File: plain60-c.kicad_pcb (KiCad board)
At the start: 2 copper layers, 284.7 x 94.2 mm, 165 parts, among them J2 ISP, J3 ai03_ud, K1 KEYSW, K10 KEYSW, K11 KEYSW, K12 KEYSW, K13 KEYSW, K14 KEYSW, K15 KEYSW, K15-1 KEYSW, K16 KEYSW, K17 KEYSW, K18 KEYSW, K19 KEYSW, K2 KEYSW, K20 KEYSW, K21 KEYSW, K22 KEYSW, K23 KEYSW, K24 KEYSW, K25 KEYSW, K26 KEYSW, K27 KEYSW, K28 KEYSW, K29 KEYSW, K3 KEYSW, K31 KEYSW, K31-1 KEYSW, K32 KEYSW, K33 KEYSW, K34 KEYSW, K35 KEYSW, K36 KEYSW, K37 KEYSW, K38 KEYSW, K39 KEYSW, K4 KEYSW, K40 KEYSW, K41 KEYSW, K42 KEYSW, K43 KEYSW, K44 KEYSW, K44-1 KEYSW, K46 KEYSW, K46-1 KEYSW, K47 KEYSW, K48 KEYSW, K49 KEYSW, K5 KEYSW, K50 KEYSW, K51 KEYSW, K52 KEYSW, K53 KEYSW, K54 KEYSW, K55 KEYSW, K56 KEYSW, K57 KEYSW, K58 KEYSW, K58-1 KEYSW, K59 KEYSW, K6 KEYSW, K61 KEYSW, K61-1 KEYSW, K62 KEYSW, K62-1 KEYSW, K63 KEYSW, K63-1 KEYSW, K67 KEYSW, K67-1 KEYSW, K7 KEYSW, K71 KEYSW, K72 KEYSW, K72-1 KEYSW, K73 KEYSW, K73-1 KEYSW, K74 KEYSW, K74-1 KEYSW, K8 KEYSW, K9 KEYSW, SW1 SW_PUSH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

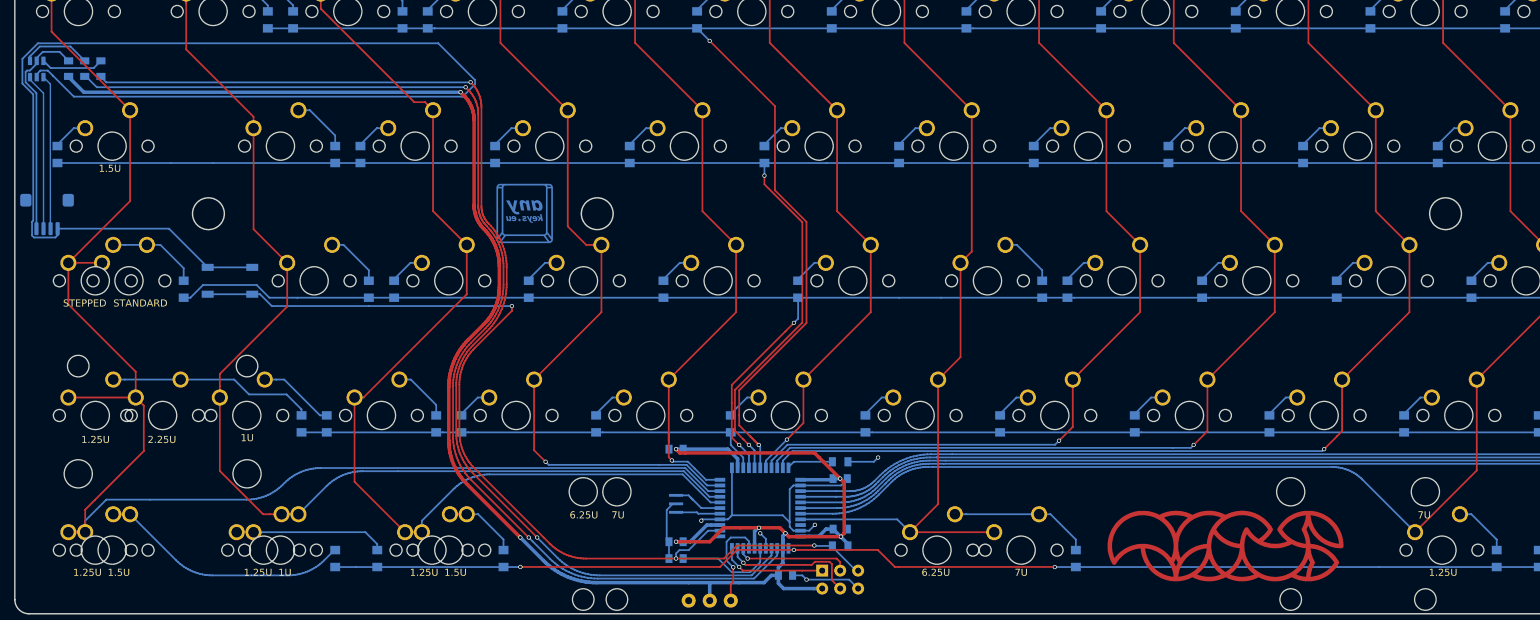
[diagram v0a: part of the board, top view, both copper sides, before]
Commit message: fixed some traces and redo gerber
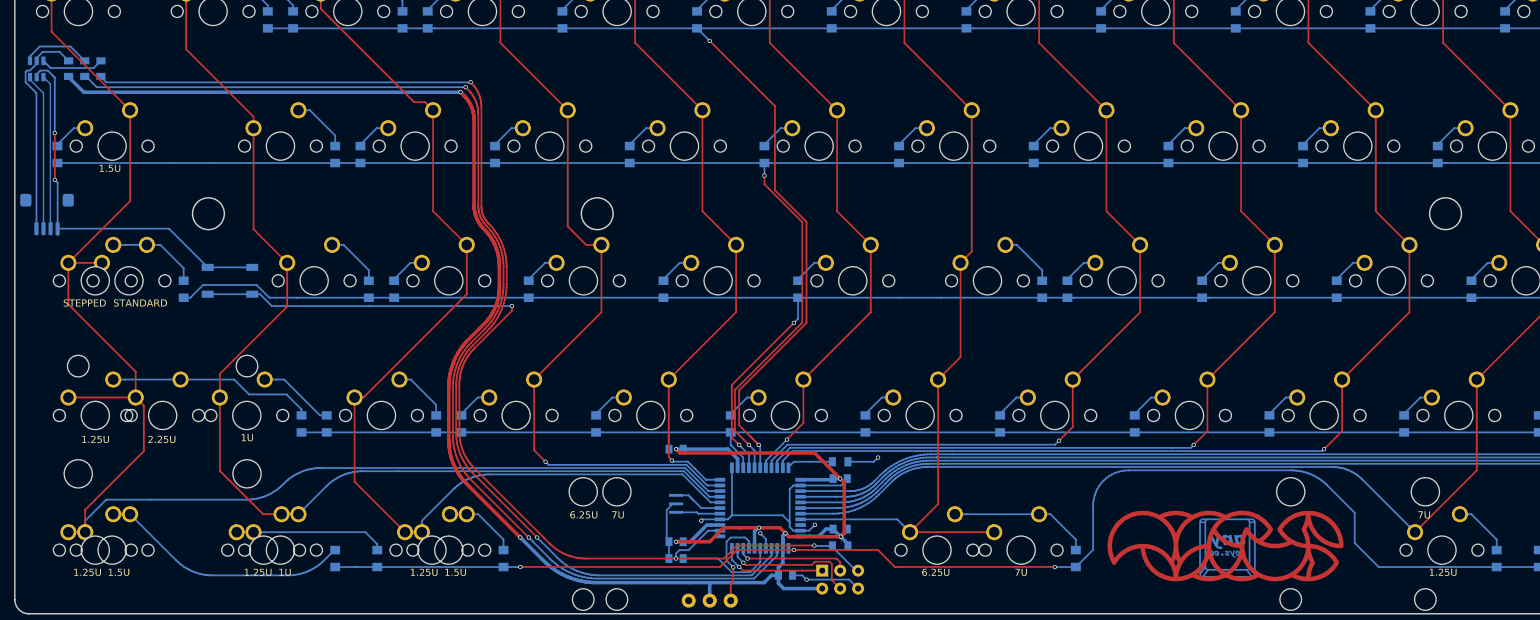
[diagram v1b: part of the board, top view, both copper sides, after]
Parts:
- moved G*** 132.4 mm to (163.1, 85.4)
- moved G*** 110.1 mm to (172.1, 85.4)
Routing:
- net GND: track 257.7 -> 120.6 mm, vias 5 -> 7
- net row4: track 196.9 -> 214.9 mm
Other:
- board text removed: "Noctus edition"

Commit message: add side cuts
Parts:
- moved G*** 0.74 mm to (163.1, 86.2)
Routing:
- net GND: track 120.6 -> 318.1 mm, vias 7 -> 11
- net row4: track 214.9 -> 234.2 mm
- net col10: track 184.7 -> 189.6 mm
- net RST: track 139.9 -> 144.0 mm
- net VCC: track 278.3 -> 275.2 mm
- net row0: track 288.2 -> 286.9 mm
- net col4: track 87.9 -> 86.6 mm
- net D+: track 21.9 -> 22.8 mm, vias 0 -> 2
- net VBUS: track 31.1 -> 30.4 mm, vias 0 -> 2
- net Net-(U1-Pad17): track 7.45 -> 6.95 mm
- net D-: vias 0 -> 2
- added copper zone on F.Cu, net (none)
- added copper zone on B.Cu, net GND
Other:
- outline, holes or cut-outs redrawn

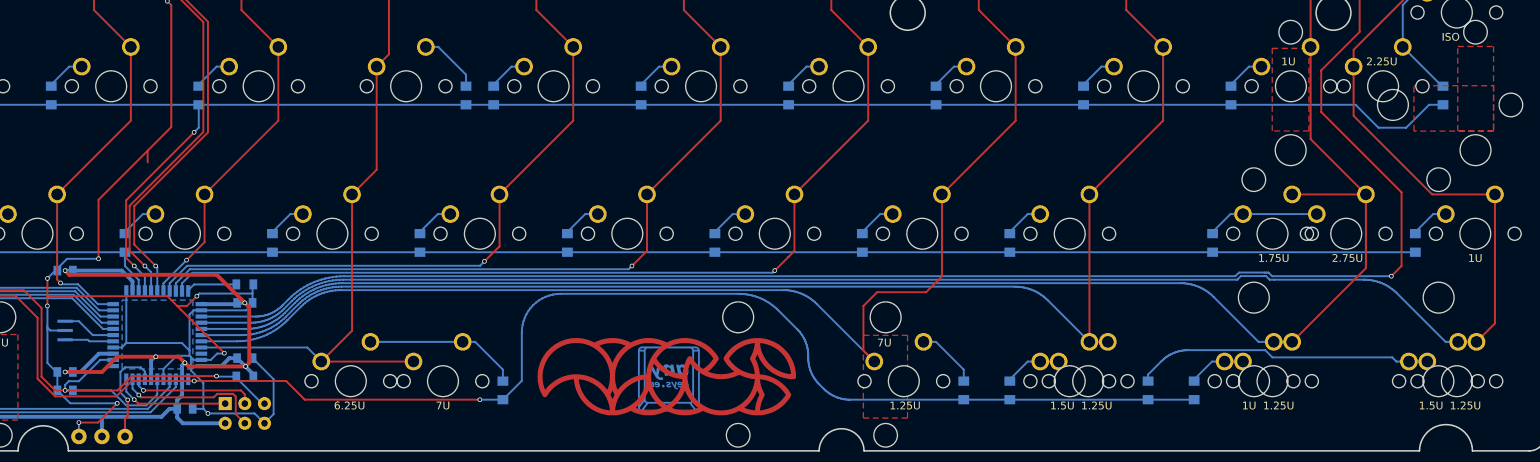
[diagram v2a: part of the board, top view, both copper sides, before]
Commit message: edited traces
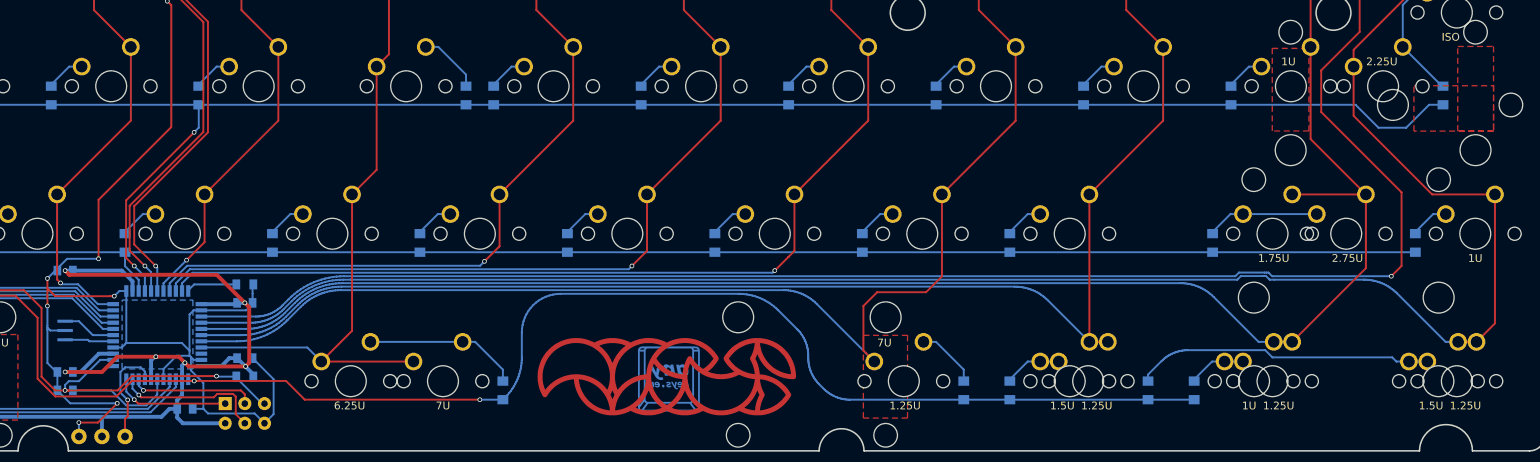
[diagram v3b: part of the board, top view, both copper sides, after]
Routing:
- net GND: track 318.1 -> 287.8 mm, vias 11 -> 9

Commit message: add cut
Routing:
- net col5: track 81.7 -> 253.8 mm
- net col6: track 114.5 -> 255.8 mm
- net row0: track 286.9 -> 407.2 mm
- net row1: track 283.8 -> 404.1 mm
- net row2: track 280.5 -> 400.5 mm
- net col4: track 86.6 -> 190.5 mm
- net col7: track 119.3 -> 214.5 mm
- net GND: track 287.8 -> 376.7 mm
- net col3: track 106.6 -> 173.4 mm
- net col8: track 137.9 -> 196.6 mm
- net col2: track 146.1 -> 124.2 mm
- net col9: track 156.2 -> 177.5 mm
- net RST: track 144.0 -> 130.9 mm
- net VCC: track 275.2 -> 264.0 mm
- net Net-(R1-Pad1): track 162.2 -> 160.8 mm
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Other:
- outline, holes or cut-outs redrawn

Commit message: fix thing
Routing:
- net col2: track 124.2 -> 167.8 mm, vias 0 -> 2
- net VCC: track 264.0 -> 264.6 mm
- net col3: track 173.4 -> 173.9 mm

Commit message: pain
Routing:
- net row2: track 400.5 -> 404.2 mm
- net row1: track 404.1 -> 406.7 mm
- net Net-(D29-Pad2): track 36.6 -> 38.7 mm
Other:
- outline, holes or cut-outs redrawn
